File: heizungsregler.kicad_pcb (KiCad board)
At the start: 2 copper layers, 65 x 65.3 mm, 78 parts, among them J102 Conn_01x03_Male, J103 Conn_01x10_Male, J301 Conn_01x02_Male, Q301 BC847, Q302 BC847, Q303 BCP51, U101 oled_0.96, U102 DS18B20, U201 ENC28J60x-SS, U202 TPS54231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

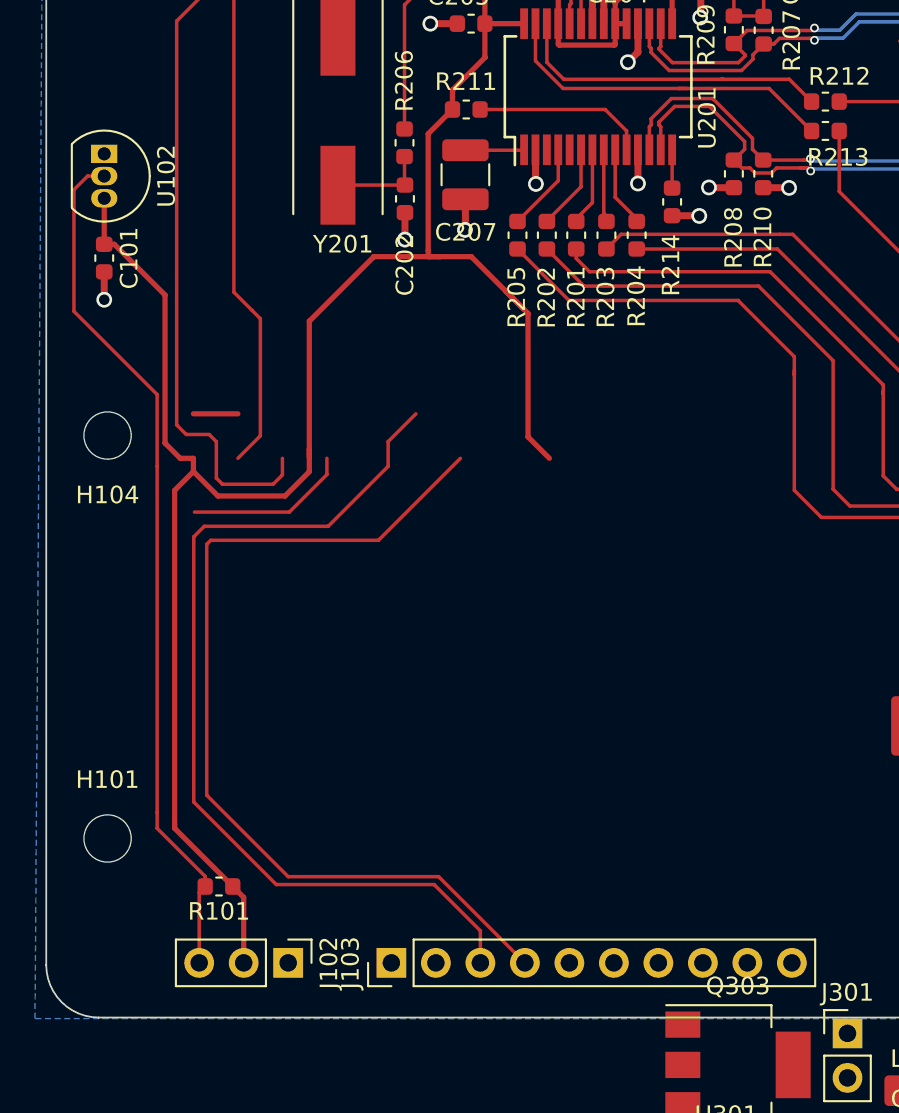
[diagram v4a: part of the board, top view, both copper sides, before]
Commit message: Relais geroutet
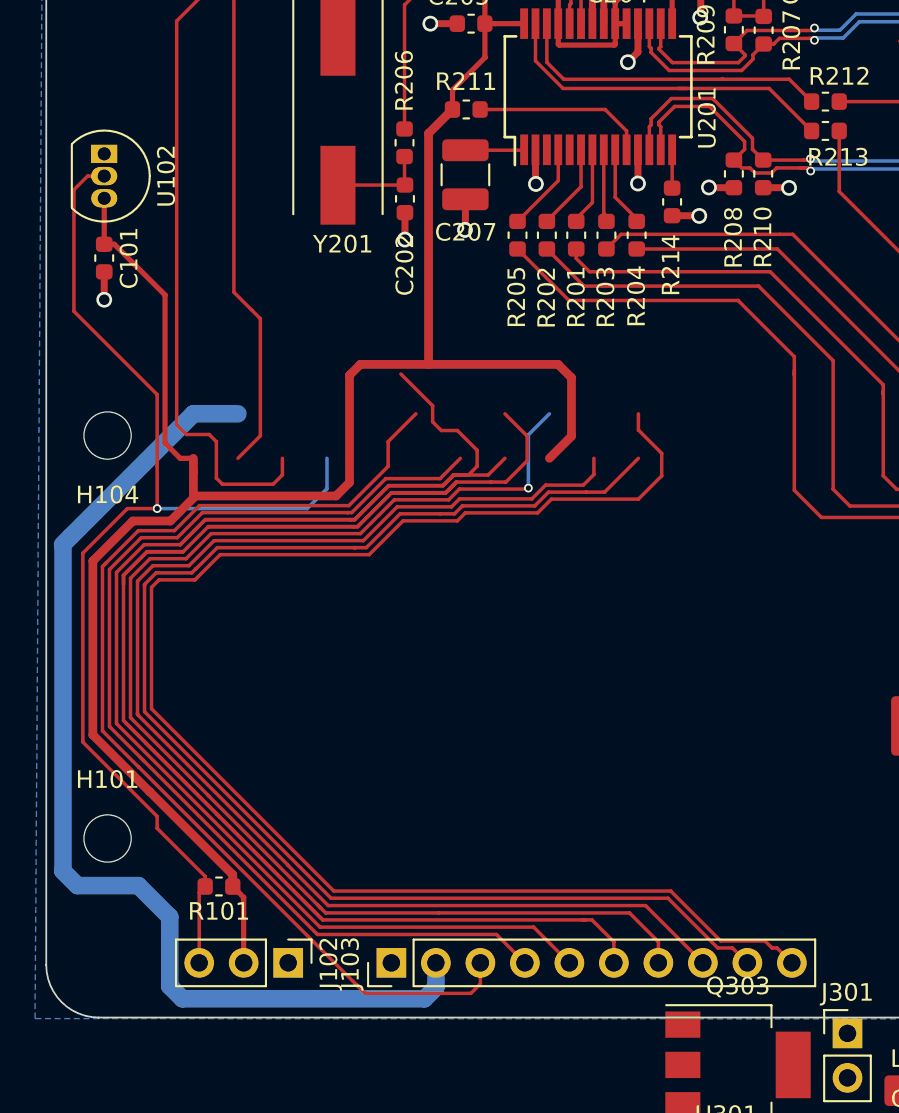
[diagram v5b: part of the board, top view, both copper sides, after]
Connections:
- J103 pad 2: +3V3 -> +5V
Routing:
- net /REL4: track 0.00 -> 107.7 mm
- net /REL3: track 0.00 -> 91.4 mm
- net /REL8: track 0.00 -> 85.3 mm
- net /REL7: track 0.00 -> 79.0 mm
- net /REL6: track 0.00 -> 75.3 mm
- net /REL5: track 0.00 -> 74.4 mm, vias 0 -> 1
- net +5V: track 2.54 -> 60.0 mm
- net /REL1: track 52.8 -> 61.3 mm
- net /REL2: track 53.0 -> 61.2 mm
- net /DQ: track 58.8 -> 65.8 mm, vias 0 -> 1
- net +3V3: track 156.2 -> 158.1 mm

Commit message: Design weiter bearbeitet
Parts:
- removed C101: C, Capacitor_SMD:C_0603_1608Metric
- removed C201, C202: 22P, Capacitor_SMD:C_0603_1608Metric
- removed C203, C204, C205, C206, C208, C212: 100N, Capacitor_SMD:C_0603_1608Metric
- removed C209: 8N2, Capacitor_SMD:C_0603_1608Metric
- removed C210: 82P, Capacitor_SMD:C_0603_1608Metric
- removed C211: 4N3, Capacitor_SMD:C_0603_1608Metric
- removed C302: 330P, Capacitor_SMD:C_0603_1608Metric
- removed D201, D301: D_Schottky, Diode_SMD:D_SOD-123
- removed F301: Fuse 2A, Fuse:Fuse_1812_4532Metric
- removed FB201: Ferrite_Bead, Inductor_SMD:L_0603_1608Metric
- removed H101, H102, H103, H104: MountingHole, MountingHole:MountingHole_2.7mm_M2.5_DIN965
- removed J102: Conn_01x03_Male, Connector_PinHeader_2.54mm:PinHeader_1x03_P2.54mm_Vertical
- removed J301: Conn_01x02_Male, Connector_PinHeader_2.54mm:PinHeader_1x02_P2.54mm_Vertical
- removed L201: 22U, Inductor_SMD:L_Bourns_SRN6045TA
- removed L301: 150U, Inductor_SMD:L_Bourns-SRN4018
- removed L302: 1U, Inductor_SMD:L_1206_3216Metric
- removed Q301, Q302: BC847, Package_TO_SOT_SMD:SOT-23
- removed Q303: BCP51, Package_TO_SOT_SMD:SOT-223
- removed R101: R, Resistor_SMD:R_0603_1608Metric
- removed R201, R202, R203, R204, R205, R206, R211, R301, R302: 0R00, Resistor_SMD:R_0603_1608Metric
- removed R207, R208, R209, R210: 49R9, Resistor_SMD:R_0603_1608Metric
- removed R212, R213: 220R, Resistor_SMD:R_0603_1608Metric
- removed R214: 2K32, Resistor_SMD:R_0603_1608Metric
- removed R215: 19K6, Resistor_SMD:R_0603_1608Metric
- removed R216: 18K7, Resistor_SMD:R_0603_1608Metric
- removed R217: 169K, Resistor_SMD:R_0603_1608Metric
- removed R218: 10K2, Resistor_SMD:R_0603_1608Metric
- removed R219: 1K96, Resistor_SMD:R_0603_1608Metric
- removed R303, R304: 1K, Resistor_SMD:R_0603_1608Metric
- removed R305: 0R47, Resistor_SMD:R_0603_1608Metric
- removed R306: 180, Resistor_SMD:R_0603_1608Metric
- removed R307: 4k7, Resistor_SMD:R_0603_1608Metric
- removed R308: 39K, Resistor_SMD:R_0603_1608Metric
- removed R309, R313: 22K, Resistor_SMD:R_0603_1608Metric
- removed R310: 100K, Resistor_SMD:R_0603_1608Metric
- removed R311: 33K, Resistor_SMD:R_0603_1608Metric
- removed R312: 3K3, Resistor_SMD:R_0603_1608Metric
- removed R314: 220K, Resistor_SMD:R_0603_1608Metric
- removed R315: 82R, Resistor_SMD:R_0603_1608Metric
- removed U102: DS18B20, Package_TO_SOT_THT:TO-92_Inline
- removed U201: ENC28J60x-SS, Package_SO:SSOP-28_5.3x10.2mm_P0.65mm
- removed U301: MC34063AD, Package_SO:SOIC-8_3.9x4.9mm_P1.27mm
- removed Y201: Crystal, Crystal:Crystal_SMD_HC49-SD
- added J101: RPi_GPIO, Connector_Samtec_HLE_THT:Samtec_HLE-120-02-xx-DV-TE_2x20_P2.54mm_Horizontal, B.Cu at (122.2, 85.0)
- C207: footprint Capacitor_SMD:C_1210_3225Metric -> Capacitor_Tantalum_SMD:CP_EIA-6032-28_Kemet-C
- C213, C215: footprint Capacitor_SMD:C_1210_3225Metric -> Capacitor_SMD:CP_Elec_5x5.4
- C214, C303: footprint Capacitor_SMD:C_1210_3225Metric -> Capacitor_SMD:CP_Elec_6.3x7.7
- C301: footprint Capacitor_SMD:C_1210_3225Metric -> Capacitor_SMD:CP_Elec_6.3x5.7
- C304: value 47U -> 1U; footprint Capacitor_SMD:C_1210_3225Metric -> Capacitor_SMD:C_1206_3216Metric
- moved U202 69.5 mm to (168.4, 101.1), turned to 270 degrees
- moved C214 57.7 mm to (168.2, 118.0)
- moved C213 53.4 mm to (174.6, 95.4)
- moved C301 29.6 mm to (142.9, 102.9)
- moved C215 29.0 mm to (174.5, 89.5)
- moved C303 26.5 mm to (139.0, 111.6)
- moved C304 19.9 mm to (144.7, 115.7)
- moved J103 14.7 mm to (123.8, 124.9)
- moved C207 1.29 mm to (137.7, 70.1)
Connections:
- C214 pad 1: GND -> Net-(C214-Pad1)
- C214 pad 2: Net-(C214-Pad2) -> GND
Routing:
- net /REL8: track 85.3 -> 42.8 mm
- net /REL7: track 79.0 -> 38.6 mm
- net +24V: track 0.00 -> 17.5 mm
- net /REL6: track 75.3 -> 88.6 mm
- net /REL4: track 107.7 -> 95.8 mm
- net /REL2: track 61.2 -> 66.6 mm
- net /REL5: track 74.4 -> 79.3 mm
- net /REL3: track 91.4 -> 88.1 mm
- net +3V3: track 158.1 -> 161.3 mm
- net /REL1: track 61.3 -> 63.3 mm
- net /DQ: track 65.8 -> 67.2 mm
- net +5V: track 60.0 -> 60.8 mm
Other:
- board size 65 x 65.3 mm -> 65.5 x 76.5 mm

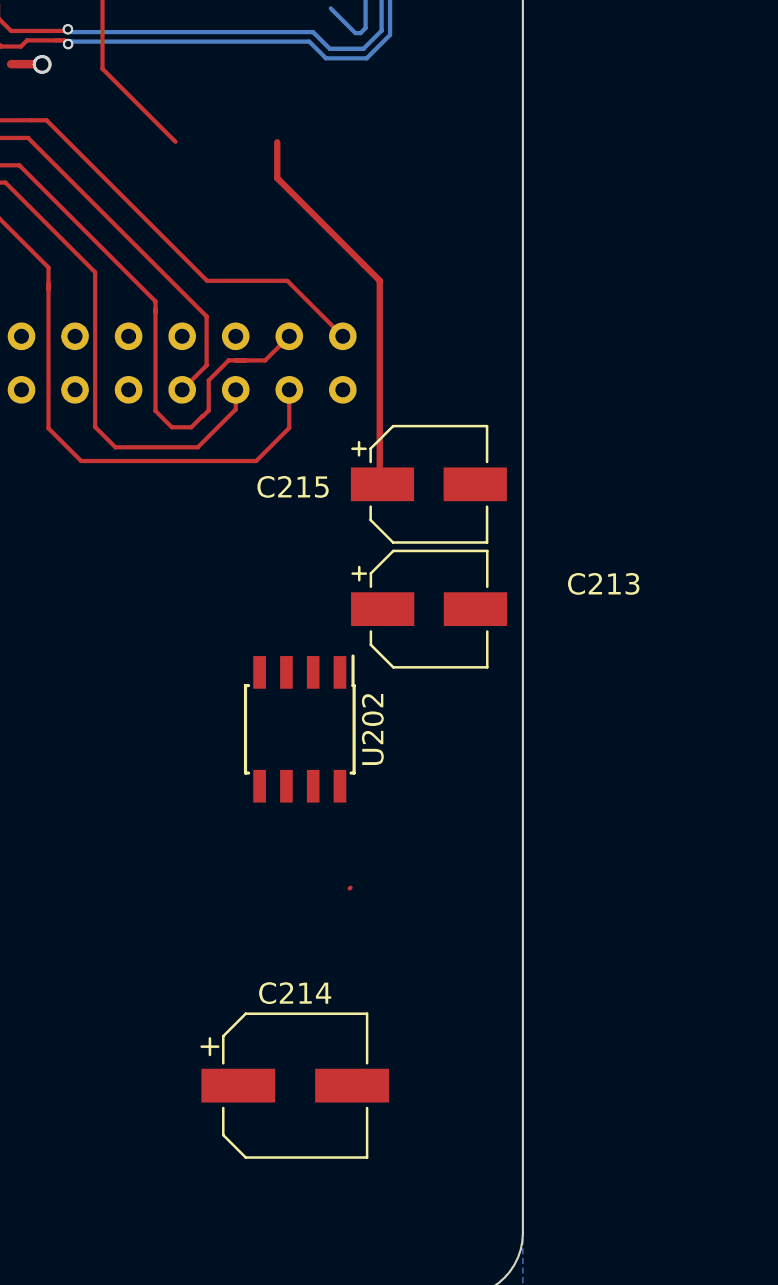
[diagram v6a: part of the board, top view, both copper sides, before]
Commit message: TPS54231 geroutet
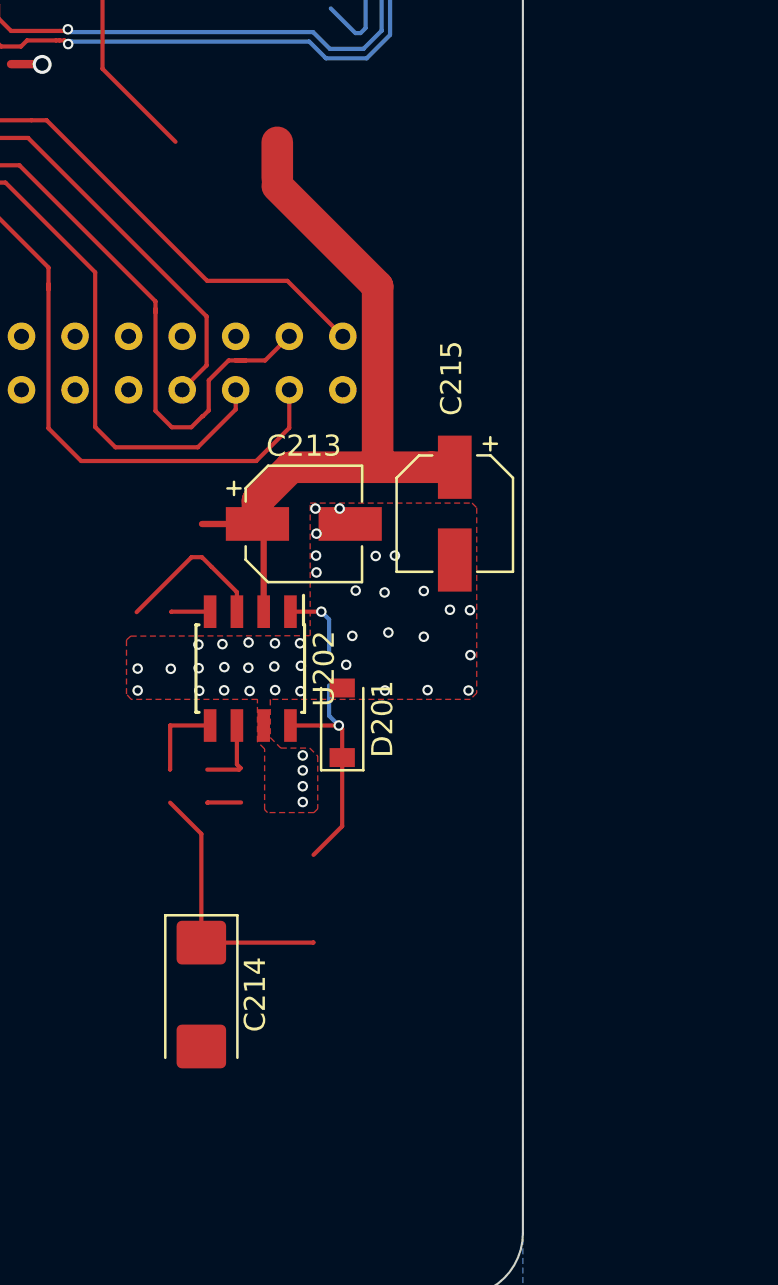
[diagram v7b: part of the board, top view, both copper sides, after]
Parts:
- added D201: D_Schottky, Diode_SMD:D_SOD-123, F.Cu at (170.4, 100.8)
- C214: footprint Capacitor_SMD:CP_Elec_6.3x7.7 -> Capacitor_Tantalum_SMD:CP_EIA-6032-28_Kemet-C
- moved C213 7.18 mm to (168.6, 91.4)
- moved C214 6.20 mm to (163.8, 113.7), turned to 270 degrees
- moved U202 3.72 mm to (166.1, 98.2)
- moved C215 1.86 mm to (175.8, 90.9), turned to 270 degrees
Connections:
- C214 pad 1: Net-(C214-Pad1) -> +5V
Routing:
- net +24V: track 17.5 -> 35.4 mm
- net +5V: track 60.8 -> 73.4 mm
- net Net-(C212-Pad1): track 0.06 -> 11.2 mm, vias 0 -> 1
- net Net-(R215-Pad2): track 0.00 -> 7.45 mm
- net Net-(R218-Pad1): track 0.00 -> 4.00 mm
- net Net-(C210-Pad2): track 0.00 -> 3.71 mm
- net Net-(C212-Pad2): track 0.00 -> 3.54 mm, vias 0 -> 1
- net Net-(C209-Pad2): track 0.00 -> 1.85 mm
- net Net-(C211-Pad1): track 0.00 -> 1.61 mm
- net GND: vias 16 -> 58
- added copper zone on F.Cu, net GND

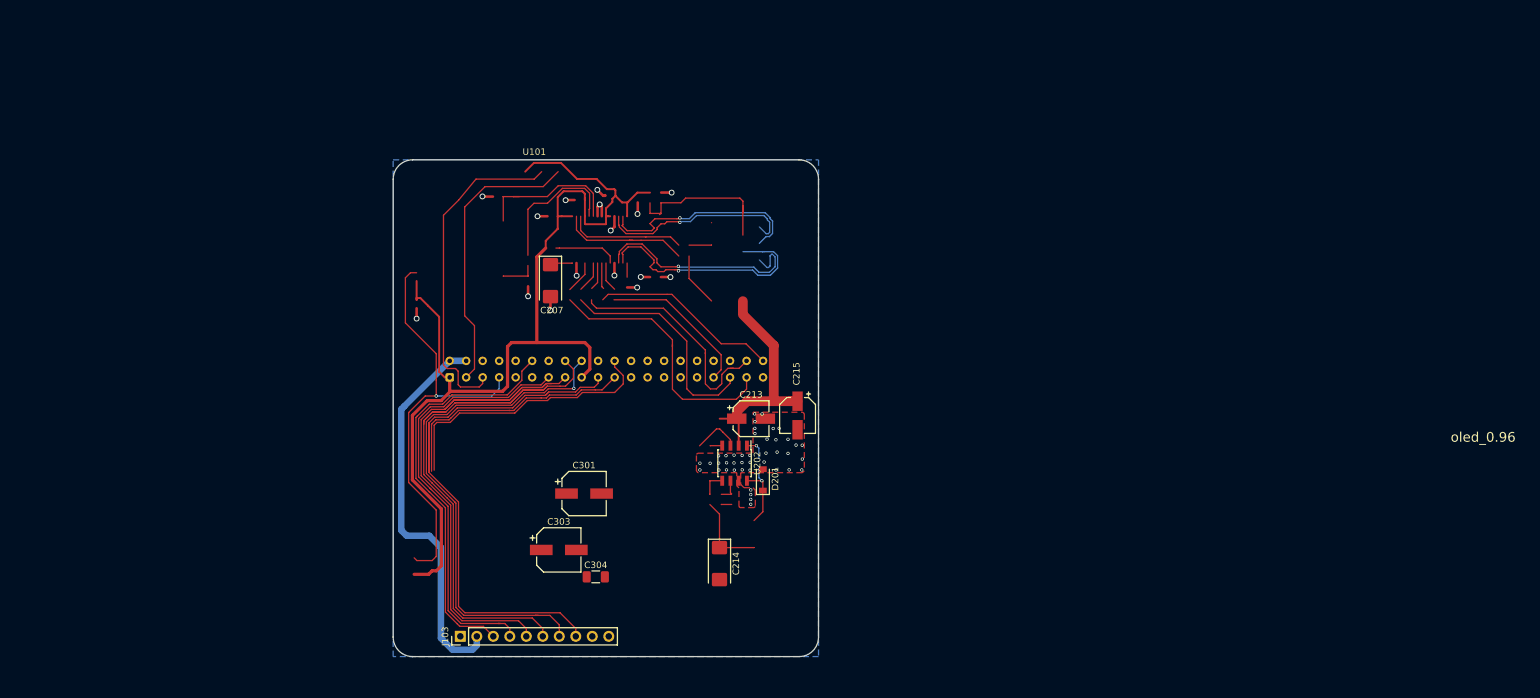
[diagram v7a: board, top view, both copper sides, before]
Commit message: Transistoren für Relais eingefügt, Pull-Ups für I2C, zusätzlicher Spannungseingang, Layout fertig
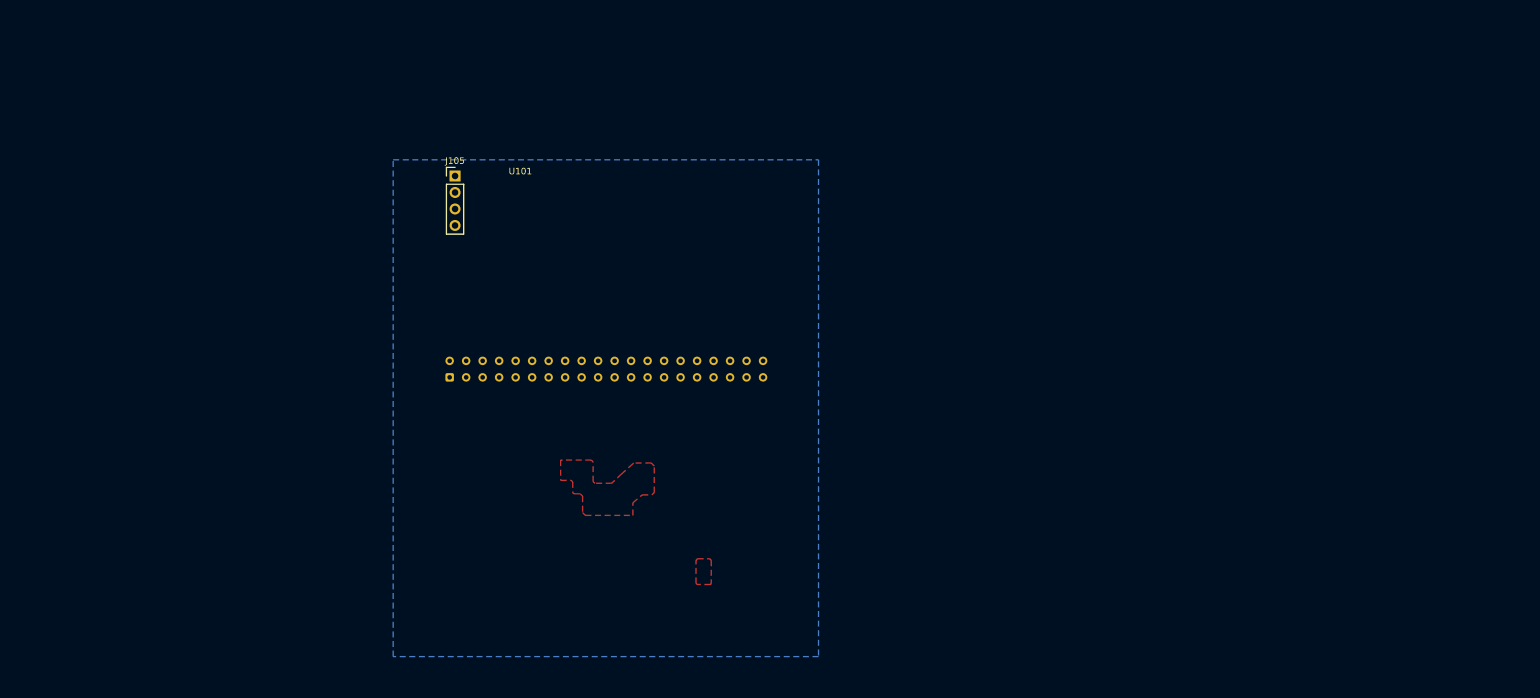
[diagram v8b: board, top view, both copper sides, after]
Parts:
- removed C207: 10U, Capacitor_Tantalum_SMD:CP_EIA-6032-28_Kemet-C
- removed C213, C215: 10U, Capacitor_SMD:CP_Elec_5x5.4
- removed C214: 47U, Capacitor_Tantalum_SMD:CP_EIA-6032-28_Kemet-C
- removed C301: 22U, Capacitor_SMD:CP_Elec_6.3x5.7
- removed C303: 47U, Capacitor_SMD:CP_Elec_6.3x7.7
- removed C304: 1U, Capacitor_SMD:C_1206_3216Metric
- removed D201: D_Schottky, Diode_SMD:D_SOD-123
- removed J103: Conn_01x10_Male, Connector_PinHeader_2.54mm:PinHeader_1x10_P2.54mm_Vertical
- removed U202: TPS54231, Package_SO:SOIC-8_3.9x4.9mm_P1.27mm
- added J105: Conn_01x04_Male, Connector_PinHeader_2.54mm:PinHeader_1x04_P2.54mm_Vertical, F.Cu at (123.0, 54.0)
- moved U101 5.73 mm to (140.8, 53.4)
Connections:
- J101 pad 17: +3V3 -> Net-(J101-Pad17)
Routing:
- net +3V3: track 161.3 -> 0.00 mm
- net /REL4: track 95.8 -> 0.00 mm
- net /REL6: track 88.6 -> 0.00 mm
- net /REL3: track 88.1 -> 0.00 mm
- net /REL5: track 79.3 -> 0.00 mm, vias 1 -> 0
- net +5V: track 73.4 -> 0.00 mm
- net /DQ: track 67.2 -> 0.00 mm, vias 1 -> 0
- net /REL2: track 66.6 -> 0.00 mm
- net /REL1: track 63.3 -> 0.00 mm
- net /SCL: track 51.0 -> 0.00 mm
- net /SDA: track 44.0 -> 0.00 mm
- net /REL8: track 42.8 -> 0.00 mm
- net /ENC_#INT: track 40.7 -> 0.00 mm
- net /REL7: track 38.6 -> 0.00 mm
- net /Ethernet/TPIN+: track 37.9 -> 0.00 mm, vias 1 -> 0
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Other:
- board outline removed
